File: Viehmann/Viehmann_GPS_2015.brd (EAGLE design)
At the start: 53.7 x 33 mm, 16 parts, among them J1 U.FL

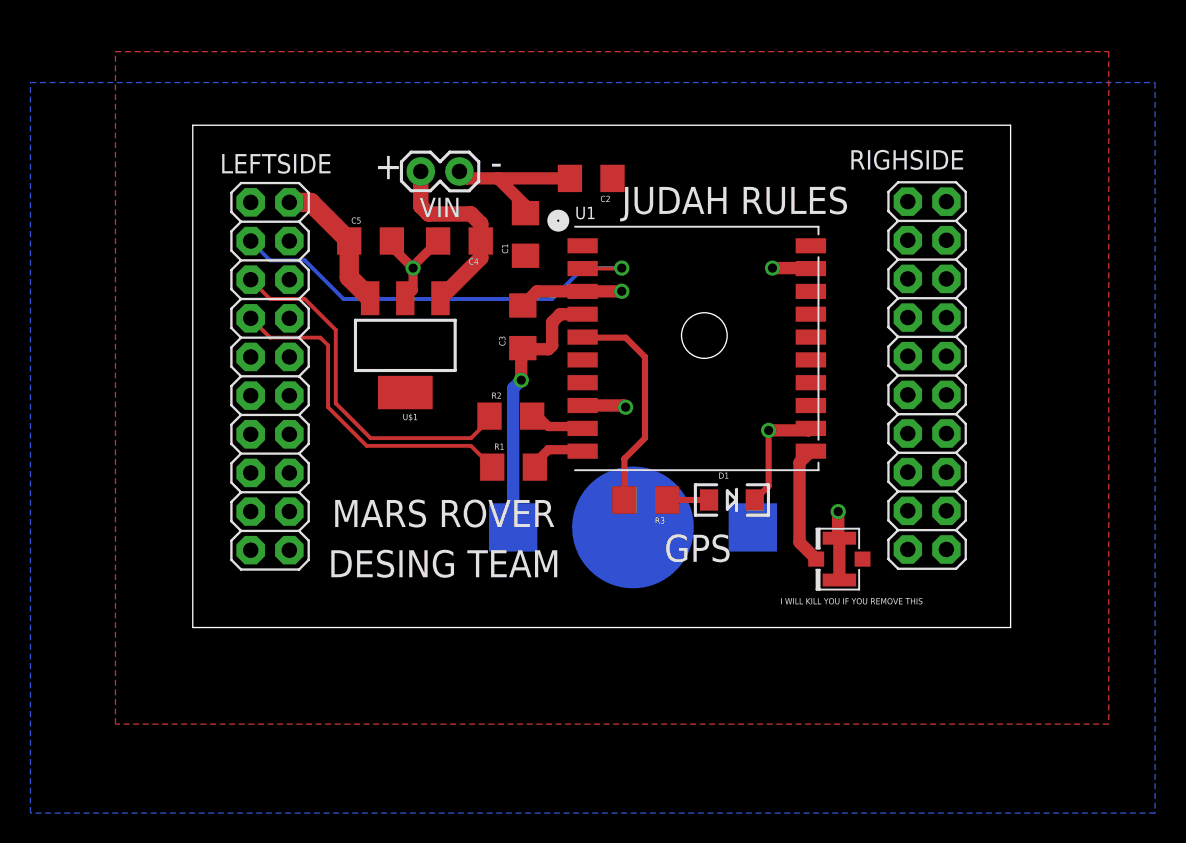
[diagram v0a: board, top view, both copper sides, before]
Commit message: Added 3-Pin Connector
Give this a look Judah and let me know if you need more stuffs
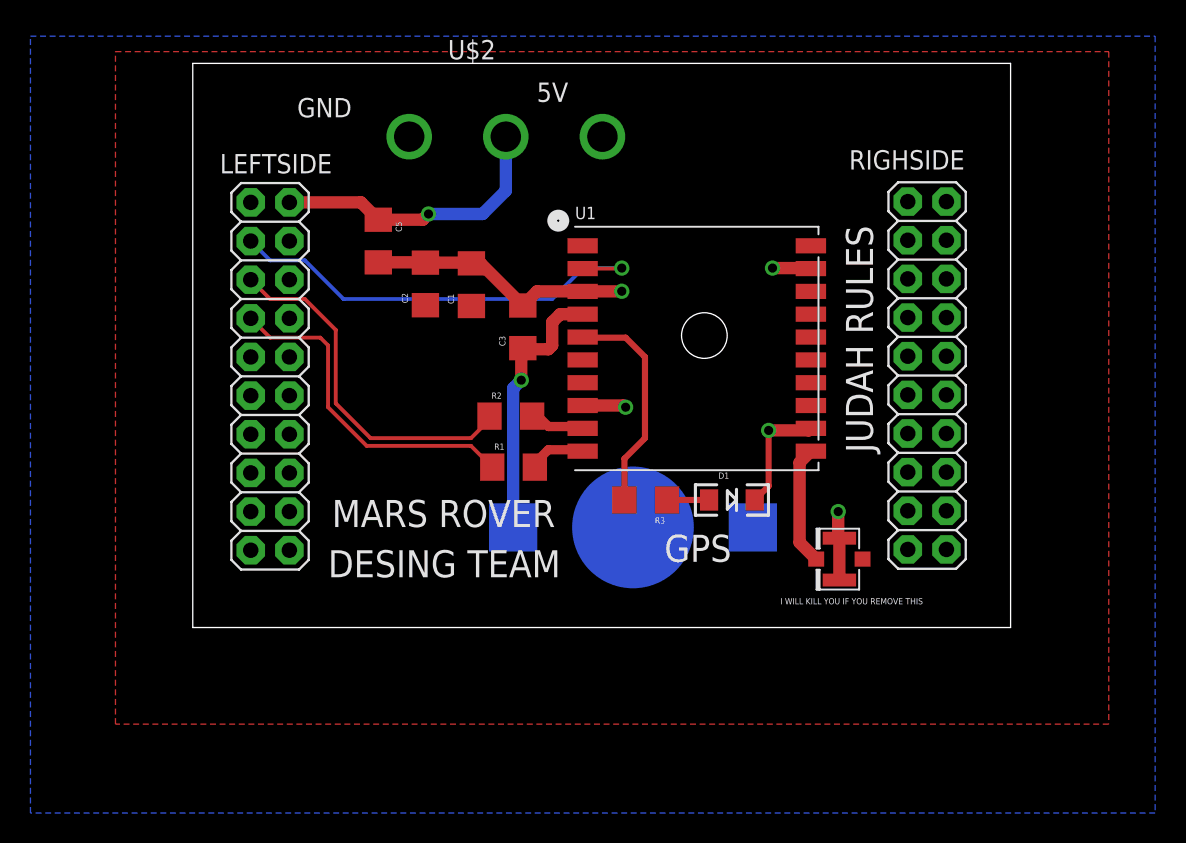
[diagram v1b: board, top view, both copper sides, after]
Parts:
- removed C4: 1uF, SparkFun-Capacitors:1206
- removed U$1: V_REG_LD1117#50, SparkFun-PowerIC:SOT223
- removed VIN: (no value), SparkFun-Connectors:1X02
- added U$2: MLX-3-PIN, MRDT-2015-General:MLX-3-PIN-SOCKET
- moved C2 12.9 mm to (15.3, 22.6), turned to 90 degrees
- moved C1 4.85 mm to (18.3, 22.5)
- moved C5 0.51 mm to (12.2, 25.4), turned to 270 degrees
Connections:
- removed net VIN: C4.1, U$1.1, VIN.1
- net 5V: now also U$2.P$2; no longer U$1.3
- net GND: now also U$2.P$1; no longer C4.2, U$1.2, VIN.2
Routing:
- net VIN: track 12.7 -> 0.00 mm
- net 5V: track 9.31 -> 19.0 mm, vias 0 -> 1
- net GND: track 42.1 -> 35.3 mm, vias 6 -> 5
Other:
- board size 53.7 x 33 mm -> 53.7 x 37.1 mm
- board text added: "5V"
- board text added: "GND"
- board text removed: "+"
- board text removed: "-"
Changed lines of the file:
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@@
 <layer number="112" name="tSilk" color="7" fill="1" visible="no" active="yes"/>
 <layer number="113" name="ReferenceLS" color="7" fill="1" visible="no" active="no"/>
+<layer number="114" name="Badge_Outline" color="7" fill="1" visible="no" active="yes"/>
+<layer number="115" name="ReferenceISLANDS" color="7" fill="1" visible="no" active="yes"/>
 <layer number="116" name="Patch_BOT" color="9" fill="4" visible="no" active="yes"/>
 <layer number="118" name="Rect_Pads" color="7" fill="1" visible="no" active="no"/>
@@
 <layer number="131" name="tAdjust" color="7" fill="1" visible="no" active="yes"/>
 <layer number="132" name="bAdjust" color="7" fill="1" visible="no" active="yes"/>
+<layer number="140" name="Page" color="7" fill="1" visible="no" active="yes"/>
+<layer number="141" name="Fabrication" color="7" fill="1" visible="no" active="yes"/>
+<layer number="142" name="AMD" color="7" fill="1" visible="no" active="yes"/>
+<layer number="143" name="PMD" color="7" fill="1" visible="no" active="yes"/>
 <layer number="144" name="Drill_legend" color="7" fill="1" visible="no" active="yes"/>
 <layer number="150" name="Notes" color="7" fill="1" visible="no" active="yes"/>
@@
 <plain>
 <wire x1="0" y1="0" x2="53.7466" y2="0" width="0" layer="20"/>
-<wire x1="53.7466" y1="0" x2="53.7466" y2="33.01" width="0" layer="20"/>
-<wire x1="53.7466" y1="33.01" x2="0" y2="33.01" width="0" layer="20"/>
-<wire x1="0" y1="33.01" x2="0" y2="0" width="0" layer="20"/>
+<wire x1="53.7466" y1="0" x2="53.7466" y2="37.074" width="0" layer="20"/>
+<wire x1="53.7466" y1="37.074" x2="0" y2="37.074" width="0" layer="20"/>
+<wire x1="0" y1="37.074" x2="0" y2="0" width="0" layer="20"/>
 <text x="38.608" y="1.524" size="0.4064" layer="25">I WILL KILL YOU IF YOU REMOVE THIS</text>
-<text x="11.938" y="29.464" size="1.778" layer="25">+</text>
-<text x="19.558" y="29.718" size="1.778" layer="25">-</text>
 <text x="9.144" y="6.604" size="1.778" layer="25">MARS ROVER </text>
 <text x="8.89" y="3.302" size="1.778" layer="25">DESING TEAM</text>
-<text x="28.194" y="27.178" size="1.778" layer="25">JUDAH RULES</text>
+<text x="42.926" y="26.416" size="1.778" layer="25" rot="R270">JUDAH RULES</text>
 <text x="30.988" y="4.318" size="1.778" layer="25">GPS</text>
+<text x="22.606" y="34.544" size="1.27" layer="21">5V</text>
+<text x="6.858" y="33.528" size="1.27" layer="21">GND</text>
 </plain>
 <attributes>
@@
 <element name="R2" library="SparkFun-Resistors" package="1206" value="330" x="20.9042" y="13.8938"/>
 <element name="R3" library="SparkFun-Resistors" package="1206" value="330" x="29.7688" y="8.382" rot="R180"/>
-<element name="C1" library="SparkFun-Capacitors" package="1206" value="1uF" x="21.8694" y="25.8318" rot="R90"/>
-<element name="C2" library="SparkFun-Capacitors" package="1206" value="0.01uF" x="26.1874" y="29.5148" rot="R180"/>
+<element name="C1" library="SparkFun-Capacitors" package="1206" value="1uF" x="18.3134" y="22.5298" rot="R90"/>
+<element name="C2" library="SparkFun-Capacitors" package="1206" value="0.01uF" x="15.2908" y="22.5806" rot="R90"/>
 <element name="C3" library="SparkFun-Capacitors" package="1206" value="1uF" x="21.6916" y="19.7612" rot="R90"/>
 <element name="D1" library="SparkFun-LED" package="LED-1206" value="" x="35.433" y="8.382"/>
@@
 <attribute name="PROD_ID" value="CONN-09193" x="-0.6858" y="46.4058" size="1.778" layer="27" rot="R180" display="off"/>
 </element>
-<element name="C4" library="SparkFun-Capacitors" package="1206" value="1uF" x="17.526" y="25.4" rot="R180"/>
-<element name="C5" library="SparkFun-Capacitors" package="1206" value="1uF" x="11.684" y="25.4"/>
-<element name="VIN" library="SparkFun-Connectors" package="1X02" value="" x="14.986" y="29.972" smashed="yes">
-<attribute name="NAME" x="14.9098" y="26.9748" size="1.27" layer="25" ratio="10"/>
-<attribute name="VALUE" x="13.716" y="26.797" size="1.27" layer="27"/>
-</element>
-<element name="U$1" library="SparkFun-PowerIC" package="SOT223" value="V_REG_LD1117#50" x="13.97" y="18.542" rot="R180"/>
+<element name="C5" library="SparkFun-Capacitors" package="1206" value="1uF" x="12.192" y="25.4" rot="R270"/>
+<element name="U$2" library="MRDT-2015-General" package="MLX-3-PIN-SOCKET" value="MLX-3-PIN" x="20.574" y="32.258"/>
 </elements>
 <signals>
 <signal name="3.3V">
-<contactref element="U1" pad="P$1"/>
-<contactref element="C2" pad="1"/>
-<contactref element="C1" pad="1"/>
-<contactref element="LEFTSIDE" pad="1"/>
 <polygon width="0.4064" layer="1">
 <vertex x="-5.08" y="37.846"/>
@@
 <vertex x="-5.08" y="-6.35"/>
 </polygon>
+<contactref element="U1" pad="P$1"/>
+<contactref element="C2" pad="1"/>
+<contactref element="C1" pad="1"/>
+<contactref element="LEFTSIDE" pad="1"/>
 </signal>
 <signal name="GND">
@@
 <contactref element="LEFTSIDE" pad="4"/>
 <contactref element="RIGHSIDE" pad="2"/>
-<contactref element="C4" pad="2"/>
-<contactref element="C5" pad="2"/>
-<contactref element="U$1" pad="2"/>
-<contactref element="VIN" pad="2"/>
 <polygon width="0.4064" layer="16">
-<vertex x="-10.668" y="35.814"/>
-<vertex x="63.246" y="35.814"/>
+<vertex x="-10.668" y="38.862"/>
+<vertex x="63.246" y="38.862"/>
 <vertex x="63.246" y="-12.192"/>
 <vertex x="-10.668" y="-12.192"/>
 </polygon>
-<via x="14.478" y="23.622" extent="1-16" drill="0.6"/>
-<wire x1="13.084" y1="25.4" x2="13.084" y2="25.016" width="0.6096" layer="1"/>
-<wire x1="13.084" y1="25.016" x2="14.478" y2="23.622" width="0.6096" layer="1"/>
-<wire x1="14.478" y1="23.622" x2="14.478" y2="23.752" width="0.6096" layer="1"/>
-<wire x1="14.478" y1="23.752" x2="16.126" y2="25.4" width="0.6096" layer="1"/>
-<wire x1="14.478" y1="23.622" x2="14.478" y2="22.1488" width="0.6096" layer="1"/>
-<wire x1="14.478" y1="22.1488" x2="13.97" y2="21.6408" width="0.6096" layer="1"/>
 <wire x1="21.6916" y1="21.1612" x2="22.6192" y2="22.0888" width="0.8128" layer="1"/>
 <wire x1="22.6192" y1="22.0888" x2="25.6216" y2="22.0888" width="0.8128" layer="1"/>
-<wire x1="24.7874" y1="29.5148" x2="20.066" y2="29.5148" width="0.8128" layer="1"/>
-<wire x1="20.066" y1="29.5148" x2="17.9832" y2="29.5148" width="0.8128" layer="1"/>
-<wire x1="17.9832" y1="29.5148" x2="17.526" y2="29.972" width="0.8128" layer="1"/>
-<wire x1="21.8694" y1="27.2318" x2="21.8694" y2="27.7114" width="0.8128" layer="1"/>
-<wire x1="21.8694" y1="27.7114" x2="20.066" y2="29.5148" width="0.8128" layer="1"/>
 <wire x1="25.6216" y1="22.0888" x2="28.1848" y2="22.0888" width="0.8128" layer="1"/>
 <wire x1="28.1848" y1="22.0888" x2="28.194" y2="22.098" width="0.8128" layer="1"/>
@@
 <wire x1="36.933" y1="8.382" x2="37.846" y2="9.295" width="0.4064" layer="1"/>
 <wire x1="37.846" y1="9.295" x2="37.846" y2="12.954" width="0.4064" layer="1"/>
+<contactref element="U$2" pad="P$1"/>
+<contactref element="C5" pad="2"/>
+<wire x1="15.2714" y1="24" x2="15.2908" y2="23.9806" width="0.8128" layer="1"/>
+<wire x1="15.2908" y1="23.9806" x2="18.2626" y2="23.9806" width="0.8128" layer="1"/>
+<wire x1="18.2626" y1="23.9806" x2="18.3134" y2="23.9298" width="0.8128" layer="1"/>
+<wire x1="18.3134" y1="23.9298" x2="18.923" y2="23.9298" width="0.8128" layer="1"/>
+<wire x1="18.923" y1="23.9298" x2="21.6916" y2="21.1612" width="0.8128" layer="1"/>
+<wire x1="15.2714" y1="24" x2="12.192" y2="24" width="0.8128" layer="1"/>
 </signal>
 <signal name="NRESET">
@@
 <wire x1="40.9692" y1="4.4968" x2="40.9692" y2="4.4958" width="0.8128" layer="1"/>
 </signal>
-<signal name="VIN">
-<contactref element="C4" pad="1"/>
-<contactref element="U$1" pad="1"/>
-<contactref element="VIN" pad="1"/>
-<wire x1="18.926" y1="25.4" x2="18.926" y2="24.2854" width="1.016" layer="1"/>
-<wire x1="18.926" y1="24.2854" x2="16.2814" y2="21.6408" width="1.016" layer="1"/>
-<wire x1="18.926" y1="25.4" x2="18.926" y2="26.54" width="1.016" layer="1"/>
-<wire x1="18.926" y1="26.54" x2="18.288" y2="27.178" width="1.016" layer="1"/>
-<wire x1="18.288" y1="27.178" x2="15.494" y2="27.178" width="1.016" layer="1"/>
-<wire x1="15.494" y1="27.178" x2="14.986" y2="27.686" width="1.016" layer="1"/>
-<wire x1="14.986" y1="27.686" x2="14.986" y2="29.972" width="1.016" layer="1"/>
-</signal>
 <signal name="5V">
 <contactref element="LEFTSIDE" pad="2"/>
+<contactref element="U$2" pad="P$2"/>
 <contactref element="C5" pad="1"/>
-<contactref element="U$1" pad="3"/>
-<wire x1="11.6586" y1="21.6408" x2="10.284" y2="23.0154" width="1.27" layer="1"/>
-<wire x1="10.284" y1="23.0154" x2="10.284" y2="25.4" width="1.27" layer="1"/>
-<wire x1="10.284" y1="25.4" x2="7.744" y2="27.94" width="1.27" layer="1"/>
-<wire x1="7.744" y1="27.94" x2="6.35" y2="27.94" width="1.27" layer="1"/>
+<wire x1="6.35" y1="27.94" x2="11.052" y2="27.94" width="0.8128" layer="1"/>
+<wire x1="11.052" y1="27.94" x2="12.192" y2="26.8" width="0.8128" layer="1"/>
+<wire x1="12.192" y1="26.8" x2="15.116" y2="26.8" width="0.8128" layer="1"/>
+<wire x1="15.116" y1="26.8" x2="15.494" y2="27.178" width="0.8128" layer="1"/>
+<via x="15.494" y="27.178" extent="1-16" drill="0.6"/>
+<wire x1="15.494" y1="27.178" x2="19.05" y2="27.178" width="0.8128" layer="16"/>
+<wire x1="19.05" y1="27.178" x2="20.574" y2="28.702" width="0.8128" layer="16"/>
+<wire x1="20.574" y1="28.702" x2="20.574" y2="32.258" width="0.8128" layer="16"/>
 </signal>
 </signals>

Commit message: swapped power conn to app45 and put backup battery on top, gen'ed gerbers
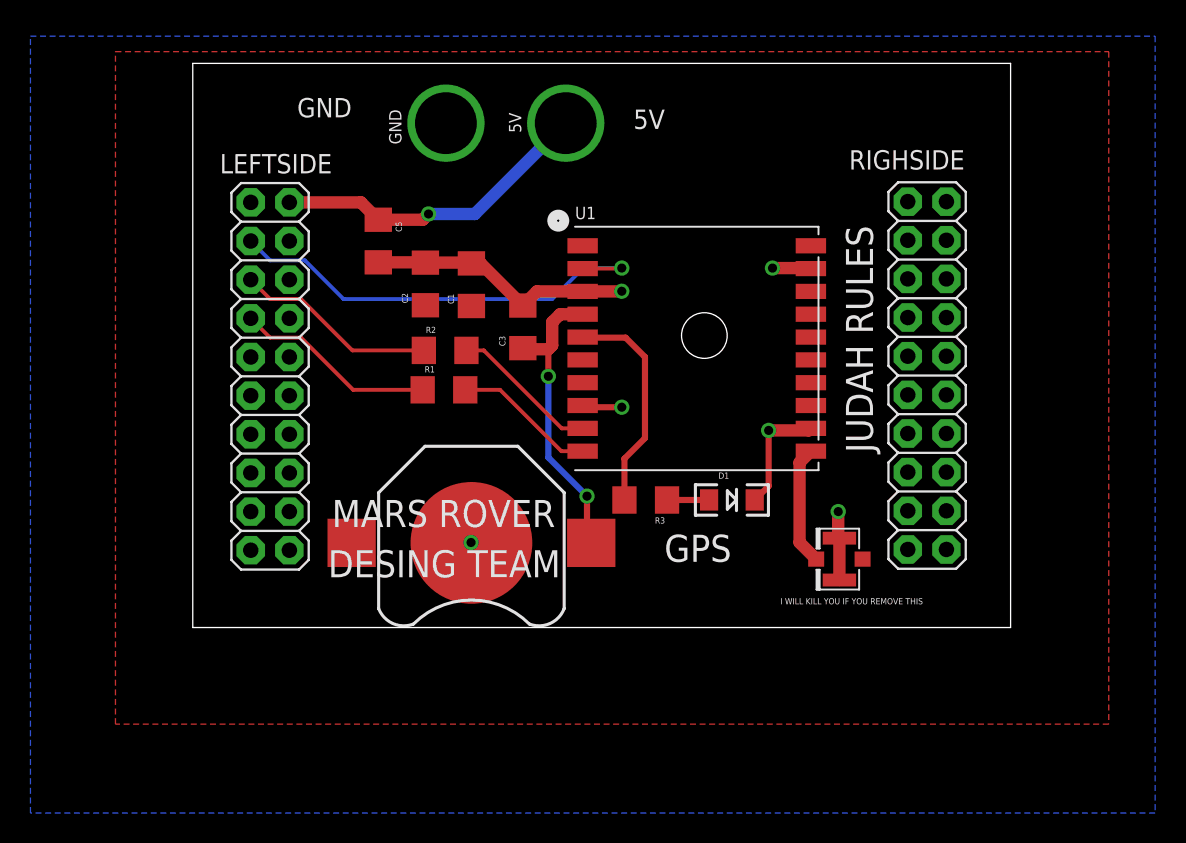
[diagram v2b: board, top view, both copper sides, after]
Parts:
- removed U$2: MLX-3-PIN, MRDT-2015-General:MLX-3-PIN-SOCKET
- added U$1: APP_2POS_CONFIG5V_VERT, MRDT-Connectors:APP45_5V_VERT_CONFIG
- moved CR1220 10.7 mm to (18.3, 5.56), flipped to the top
- moved R1 6.83 mm to (16.5, 15.6)
- moved R2 6.11 mm to (16.6, 18.2)
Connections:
- net 5V: now also U$1.5V; no longer U$2.P$2
- net GND: now also U$1.GND; no longer U$2.P$1
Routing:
- net DATA_OUT: track 23.6 -> 13.3 mm
- net DATA_IN: track 22.3 -> 13.2 mm
- net N$3: track 3.65 -> 9.76 mm
- net N$4: track 3.80 -> 9.38 mm
- net 5V: track 19.0 -> 21.3 mm
- net VBACKUP: track 17.9 -> 19.7 mm, vias 1 -> 2
- net GND: track 35.3 -> 35.0 mm, vias 5 -> 6
